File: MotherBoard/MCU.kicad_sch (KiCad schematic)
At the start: 47 parts, among them J201 Conn_ARM_SWD_TagConnect_TC2030, J202 DM3AT-SF-PEJM5_40_, U201 STM32F205RBTx, Y201 16 Mhz

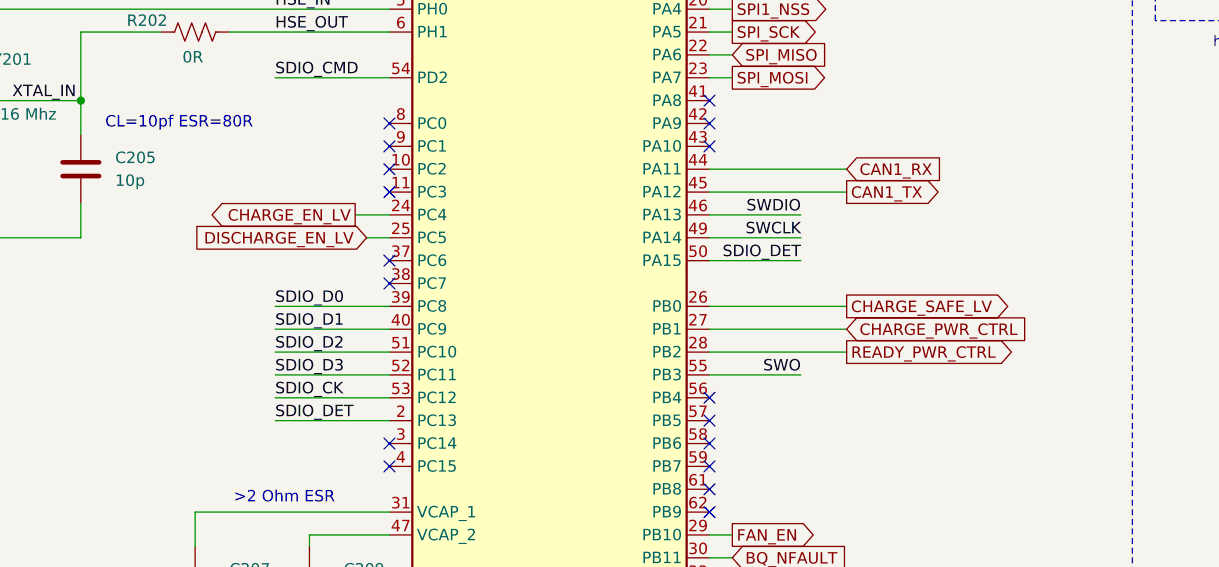
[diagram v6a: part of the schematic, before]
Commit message: Revised all schematics + completed relay driver page
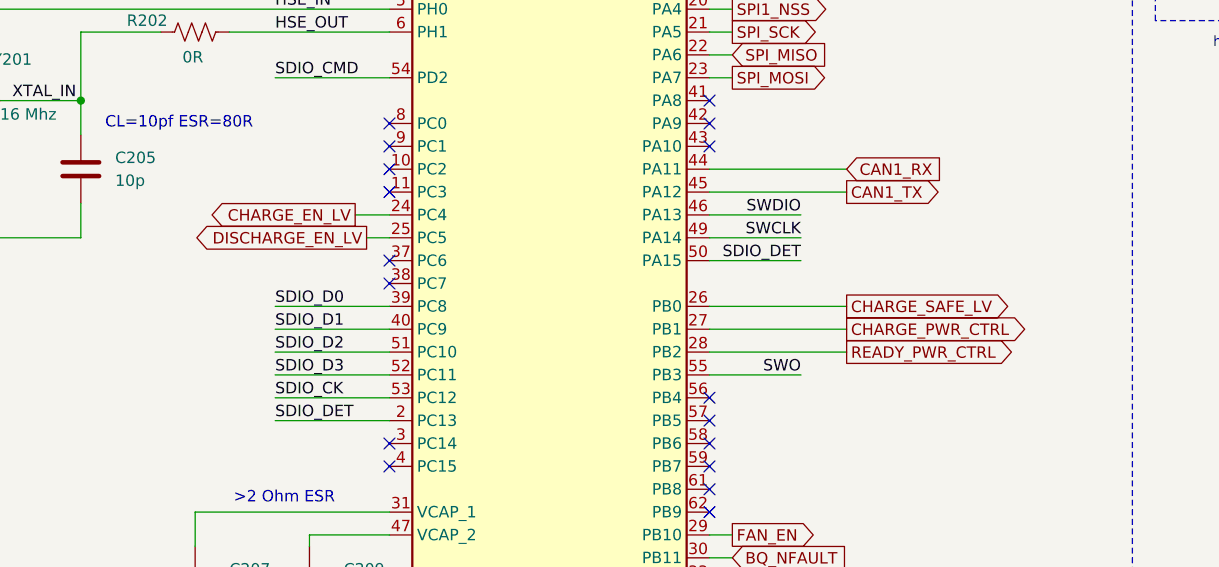
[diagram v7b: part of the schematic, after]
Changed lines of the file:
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@@
 	(title_block
 		(title "STM32 Layout")
-		(date "2025-01-08")
+		(date "2025-01-10")
 		(rev "A")
 		(company "FSAE LSU")
@@
 	)
 	(global_label "DISCHARGE_EN_LV"
-		(shape input)
+		(shape output)
 		(at 78.74 128.27 180)
 		(fields_autoplaced yes)
@@
 	)
 	(global_label "CHARGE_PWR_CTRL"
-		(shape input)
+		(shape output)
 		(at 132.08 138.43 0)
 		(fields_autoplaced yes)

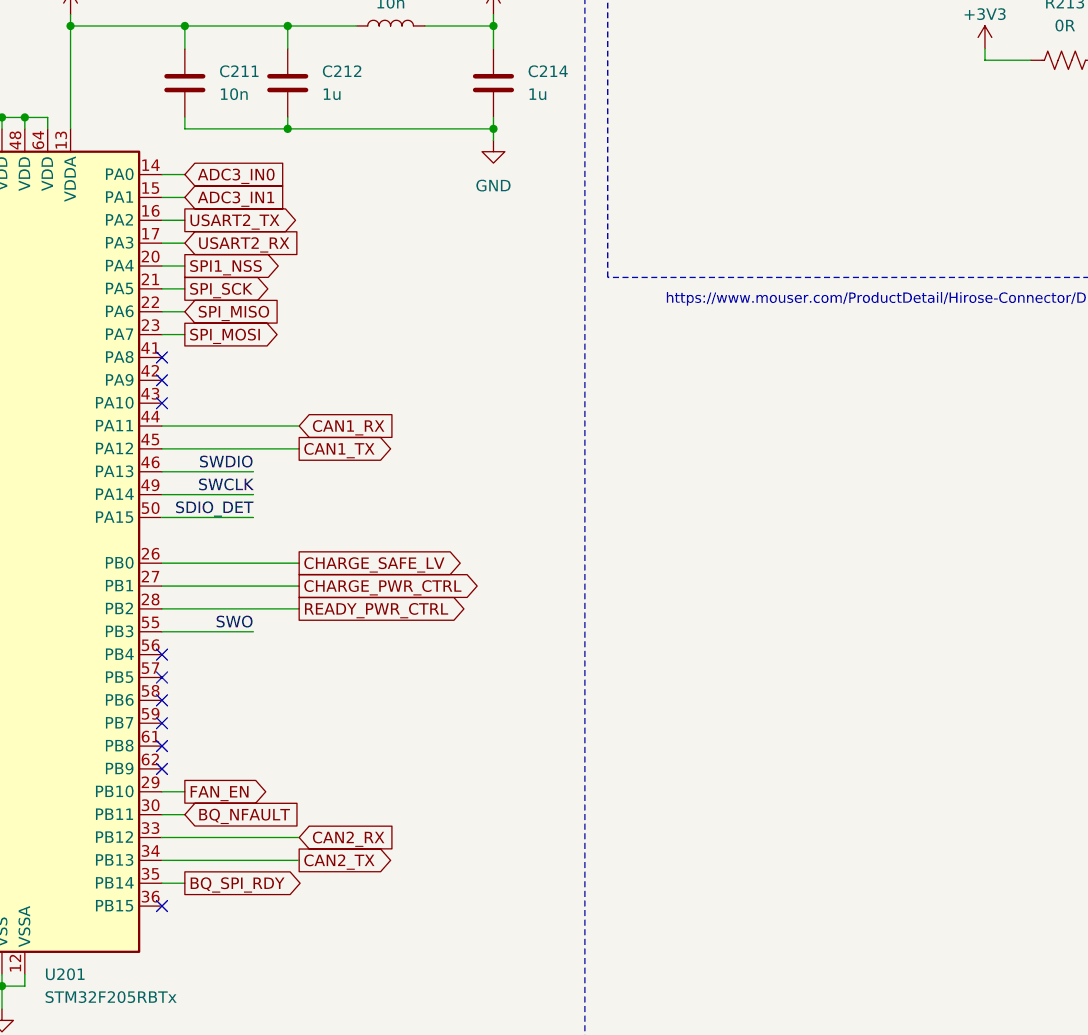
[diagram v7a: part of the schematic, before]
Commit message: Fixed 3D model paths. Finished PSU ORing shcematic.
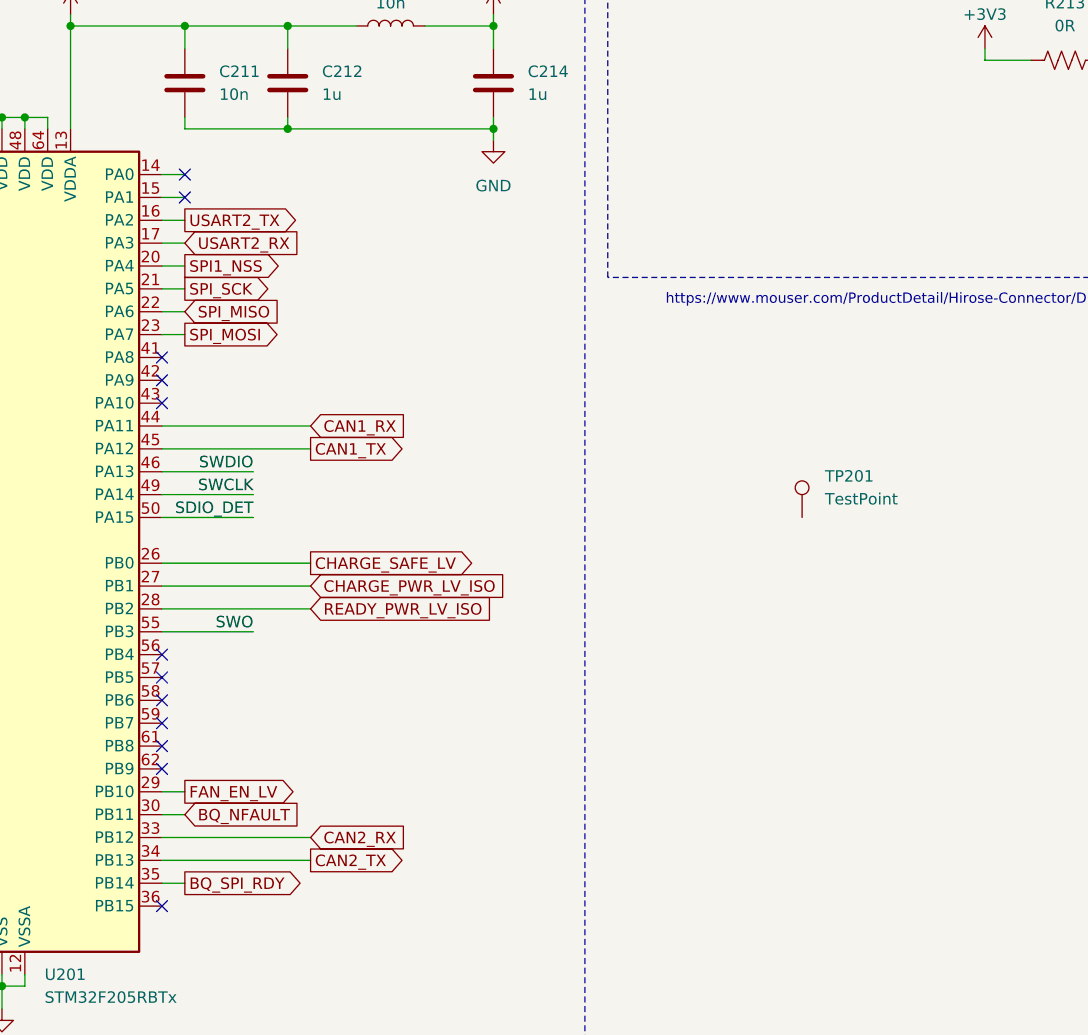
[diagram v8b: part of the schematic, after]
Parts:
- added TP201: TestPoint, TestPoint:TP_5012, symbol Connector:TestPoint
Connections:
- net ADC3_IN0: no longer names the net of U201.14 (PA0)
- net ADC3_IN1: no longer names the net of U201.15 (PA1)
- net CHARGE_PWR_CTRL renamed CHARGE_PWR_LV_ISO
- net FAN_EN renamed FAN_EN_LV
- net READY_PWR_CTRL renamed READY_PWR_LV_ISO
- no-connect marks 18 -> 20
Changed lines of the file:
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@@
 	)
 	(no_connect
+		(at 119.38 95.25)
+	)
+	(no_connect
 		(at 116.84 115.57)
 	)
@@
 	)
 	(no_connect
+		(at 119.38 92.71)
+	)
+	(no_connect
 		(at 116.84 153.67)
 	)
@@
 	(wire
 		(pts
-			(xy 116.84 166.37) (xy 132.08 166.37)
+			(xy 116.84 166.37) (xy 133.35 166.37)
 		)
 		(stroke
@@
 	(wire
 		(pts
-			(xy 116.84 138.43) (xy 132.08 138.43)
+			(xy 116.84 138.43) (xy 133.35 138.43)
 		)
 		(stroke
@@
 	(wire
 		(pts
-			(xy 132.08 140.97) (xy 116.84 140.97)
+			(xy 133.35 140.97) (xy 116.84 140.97)
 		)
 		(stroke
@@
 	(wire
 		(pts
-			(xy 116.84 123.19) (xy 132.08 123.19)
+			(xy 116.84 123.19) (xy 133.35 123.19)
 		)
 		(stroke
@@
 	(wire
 		(pts
-			(xy 116.84 168.91) (xy 132.08 168.91)
+			(xy 116.84 168.91) (xy 133.35 168.91)
 		)
 		(stroke
@@
 	(wire
 		(pts
-			(xy 116.84 120.65) (xy 132.08 120.65)
+			(xy 116.84 120.65) (xy 133.35 120.65)
 		)
 		(stroke
@@
 	(wire
 		(pts
-			(xy 116.84 135.89) (xy 132.08 135.89)
+			(xy 116.84 135.89) (xy 133.35 135.89)
 		)
 		(stroke
@@
 		)
 	)
-	(global_label "ADC3_IN0"
-		(shape input)
-		(at 119.38 92.71 0)
-		(fields_autoplaced yes)
-		(effects
-			(font
-				(size 1.27 1.27)
-			)
-			(justify left)
-		)
-		(property "Intersheetrefs" "${INTERSHEET_REFS}"
-			(at 131.3157 92.71 0)
-			(effects
-				(font
-					(size 1.27 1.27)
-				)
-				(justify left)
-				(hide yes)
-			)
-		)
-	)
 	(global_label "SPI_MOSI"
 		(shape output)
@@
 	(global_label "CAN1_RX"
 		(shape input)
-		(at 132.08 120.65 0)
+		(at 133.35 120.65 0)
 		(fields_autoplaced yes)
 		(effects
@@
 		)
 		(property "Intersheetrefs" "${INTERSHEET_REFS}"
-			(at 143.4109 120.65 0)
+			(at 144.6809 120.65 0)
 			(effects
 				(font
@@
 		)
 	)
-	(global_label "FAN_EN"
+	(global_label "FAN_EN_LV"
 		(shape output)
 		(at 119.38 161.29 0)
@@
 		)
 		(property "Intersheetrefs" "${INTERSHEET_REFS}"
-			(at 129.32 161.29 0)
+			(at 132.4043 161.29 0)
 			(effects
 				(font
@@
 	(global_label "CAN1_TX"
 		(shape output)
-		(at 132.08 123.19 0)
-		(fields_autoplaced yes)
-		(effects
-			(font
-				(size 1.27 1.27)
-			)
-			(justify left)
-		)
-		(property "Intersheetrefs" "${INTERSHEET_REFS}"
-			(at 143.1085 123.19 0)
-			(effects
-				(font
-					(size 1.27 1.27)
-				)
-				(justify left)
-				(hide yes)
-			)
-		)
-	)
-	(global_label "READY_PWR_CTRL"
-		(shape output)
-		(at 132.08 140.97 0)
+		(at 133.35 123.19 0)
 		(fields_autoplaced yes)
 		(effects
@@
 		)
 		(property "Intersheetrefs" "${INTERSHEET_REFS}"
-			(at 151.3937 140.97 0)
+			(at 144.3785 123.19 0)
 			(effects
 				(font
@@
 		)
 	)
-	(global_label "ADC3_IN1"
-		(shape input)
-		(at 119.38 95.25 0)
-		(fields_autoplaced yes)
-		(effects
-			(font
-				(size 1.27 1.27)
-			)
-			(justify left)
-		)
-		(property "Intersheetrefs" "${INTERSHEET_REFS}"
-			(at 131.3157 95.25 0)
-			(effects
-				(font
-					(size 1.27 1.27)
-				)
-				(justify left)
-				(hide yes)
-			)
-		)
-	)
 	(global_label "SPI_MISO"
 		(shape input)
@@
 	(global_label "CHARGE_SAFE_LV"
 		(shape output)
-		(at 132.08 135.89 0)
+		(at 133.35 135.89 0)
 		(fields_autoplaced yes)
 		(effects
@@
 		)
 		(property "Intersheetrefs" "${INTERSHEET_REFS}"
-			(at 151.0309 135.89 0)
+			(at 152.3009 135.89 0)
 			(effects
 				(font
@@
 		)
 	)
-	(global_label "CHARGE_PWR_CTRL"
-		(shape output)
-		(at 132.08 138.43 0)
+	(global_label "CHARGE_PWR_LV_ISO"
+		(shape input)
+		(at 133.35 138.43 0)
 		(fields_autoplaced yes)
 		(effects
@@
 		)
 		(property "Intersheetrefs" "${INTERSHEET_REFS}"
-			(at 152.9056 138.43 0)
+			(at 155.869 138.43 0)
 			(effects
 				(font
@@
 	(global_label "CAN2_TX"
 		(shape output)
-		(at 132.08 168.91 0)
+		(at 133.35 168.91 0)
 		(fields_autoplaced yes)
 		(effects
@@
 		)
 		(property "Intersheetrefs" "${INTERSHEET_REFS}"
-			(at 143.1085 168.91 0)
+			(at 144.3785 168.91 0)
 			(effects
 				(font
@@
 	(global_label "CAN2_RX"
 		(shape input)
-		(at 132.08 166.37 0)
+		(at 133.35 166.37 0)
 		(fields_autoplaced yes)
 		(effects
@@
 		)
 		(property "Intersheetrefs" "${INTERSHEET_REFS}"
-			(at 143.4109 166.37 0)
+			(at 144.6809 166.37 0)
+			(effects
+				(font
+					(size 1.27 1.27)
+				)
+				(justify left)
+				(hide yes)
+			)
+		)
+	)
+	(global_label "READY_PWR_LV_ISO"
+		(shape input)
+		(at 133.35 140.97 0)
+		(fields_autoplaced yes)
+		(effects
+			(font
+				(size 1.27 1.27)
+			)
+			(justify left)
+		)
+		(property "Intersheetrefs" "${INTERSHEET_REFS}"
+			(at 154.3571 140.97 0)
 			(effects
 				(font
@@
 					(unit 1)
 				)
+			)
+		)
+	)
+	(symbol
+		(lib_id "Connector:TestPoint")
+		(at 187.96 130.81 0)
+		(unit 1)
+		(exclude_from_sim no)
+		(in_bom yes)
+		(on_board yes)
+		(dnp no)
+		(fields_autoplaced yes)
+		(property "Reference" "TP201"
+			(at 190.5 126.2379 0)
+			(effects
+				(font
+					(size 1.27 1.27)
+				)
+				(justify left)
+			)
+		)
+		(property "Value" "TestPoint"
+			(at 190.5 128.7779 0)
+			(effects
+				(font
+					(size 1.27 1.27)
+				)
+				(justify left)
+			)
+		)
+		(property "Footprint" "TestPoint:TP_5012"
+			(at 193.04 130.81 0)
+			(effects
+				(font
+					(size 1.27 1.27)
+				)
+				(hide yes)
+			)
+		)
+		(property "Datasheet" "~"
+			(at 193.04 130.81 0)
+			(effects
+				(font
+					(size 1.27 1.27)
+				)
+				(hide yes)
+			)
+		)
+		(property "Description" "test point"
+			(at 187.96 130.81 0)
+			(effects
+				(font
+					(size 1.27 1.27)
+				)
+				(hide yes)
+			)
+		)
+		(pin "1"
+		)
+		(instances
+			(project ""
+				(path "/335e81e9-b957-4266-8116-dde74329bfca/592735c9-cbc0-4c76-b37a-83bb0c07029e"
+					(reference "TP201")
+					(unit 1)
+				)
